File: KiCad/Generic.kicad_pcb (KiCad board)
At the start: 2 copper layers, 19 x 29 mm, 16 parts, among them J1 Connector, J2 USB-C, J3 VBUS, U1 ESP32-WROOM-32, U2 FT231XQ

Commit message: Improve fab diagram
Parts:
- moved Reg1 0.75 mm to (125.2, 107.5)
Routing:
- net GND: track 82.4 -> 85.7 mm
- net +3V3: track 74.9 -> 75.9 mm

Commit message: Slight tidy of tracks
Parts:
- J1: footprint RevK:Molex_MiniSPOX_H6RA -> RevK:Molex_MiniSPOX_H6RA_0.1
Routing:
- net O: track 18.4 -> 34.4 mm
- net EN: track 46.8 -> 32.0 mm
- net GND: track 85.7 -> 95.4 mm
- net Net-(U1-Pad13): track 3.91 -> 0.00 mm, vias 1 -> 0
- net +3V3: track 75.9 -> 74.6 mm
- net IO4: track 12.7 -> 13.4 mm
- net IO3: track 8.79 -> 9.42 mm
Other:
- board text added: "2021-05-11"
- board text added: "Link to DC"
- board text removed: "Link to 5V"

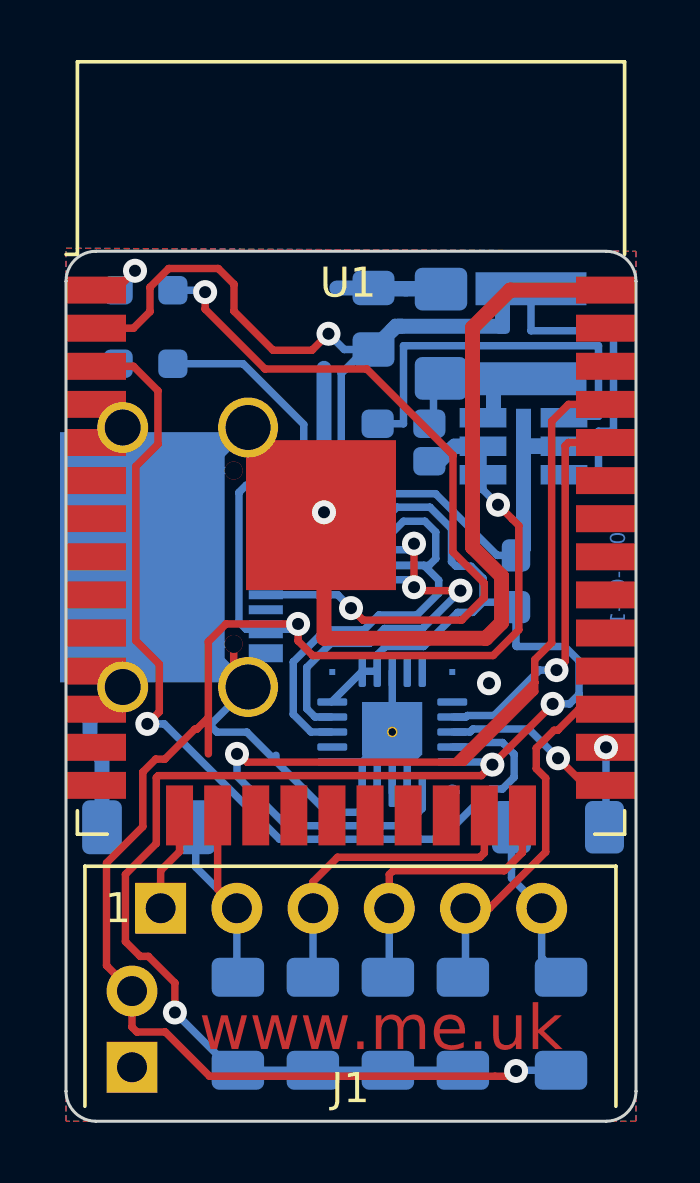
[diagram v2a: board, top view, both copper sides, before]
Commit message: Reworked for ULP pins and ADC pins
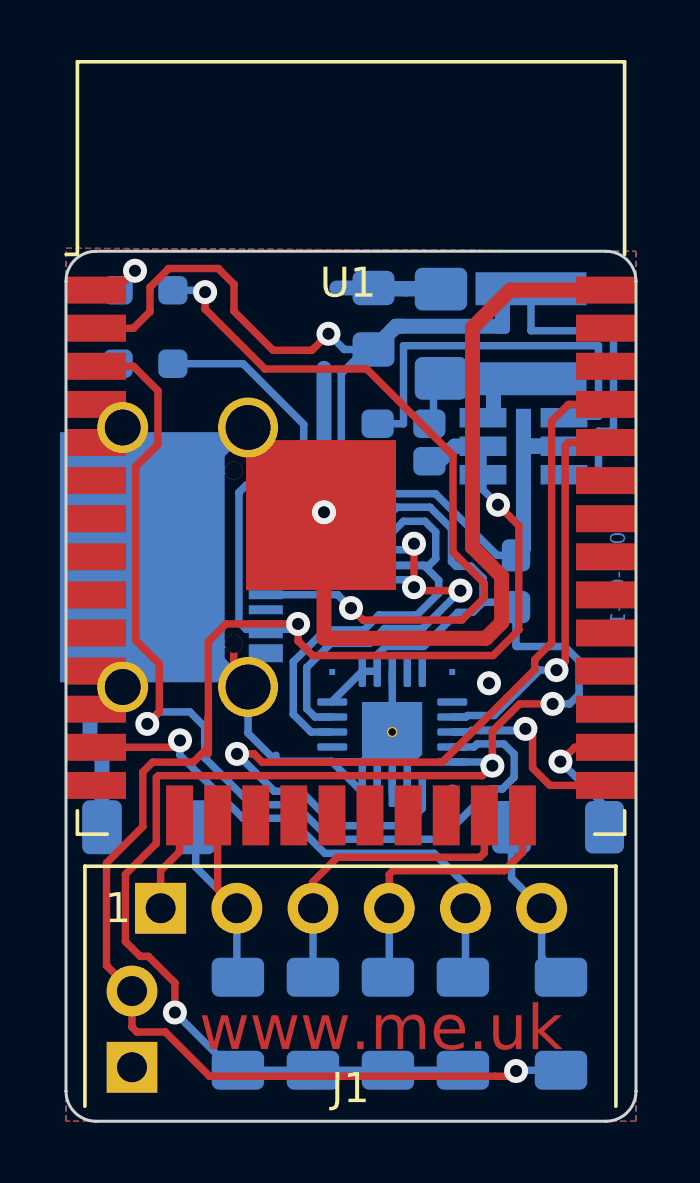
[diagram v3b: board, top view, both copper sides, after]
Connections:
- U1 pad 13: Net-(U1-Pad13) -> IO4
- U1 pad 27: IO4 -> Net-(U1-Pad27)
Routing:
- net IO4: track 13.4 -> 19.0 mm, vias 0 -> 1
- net O: track 34.4 -> 29.8 mm
- net GND: track 95.4 -> 92.9 mm
- net GPIO0: track 5.92 -> 8.30 mm
- net IO5: track 2.69 -> 4.51 mm
- net EN: track 32.0 -> 32.9 mm
- net +3V3: track 74.6 -> 75.3 mm
- net VBUS: track 57.8 -> 58.4 mm
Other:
- board text added: "14"
- board text removed: "16"

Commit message: Multi size pads with no solder past for user fit passives.
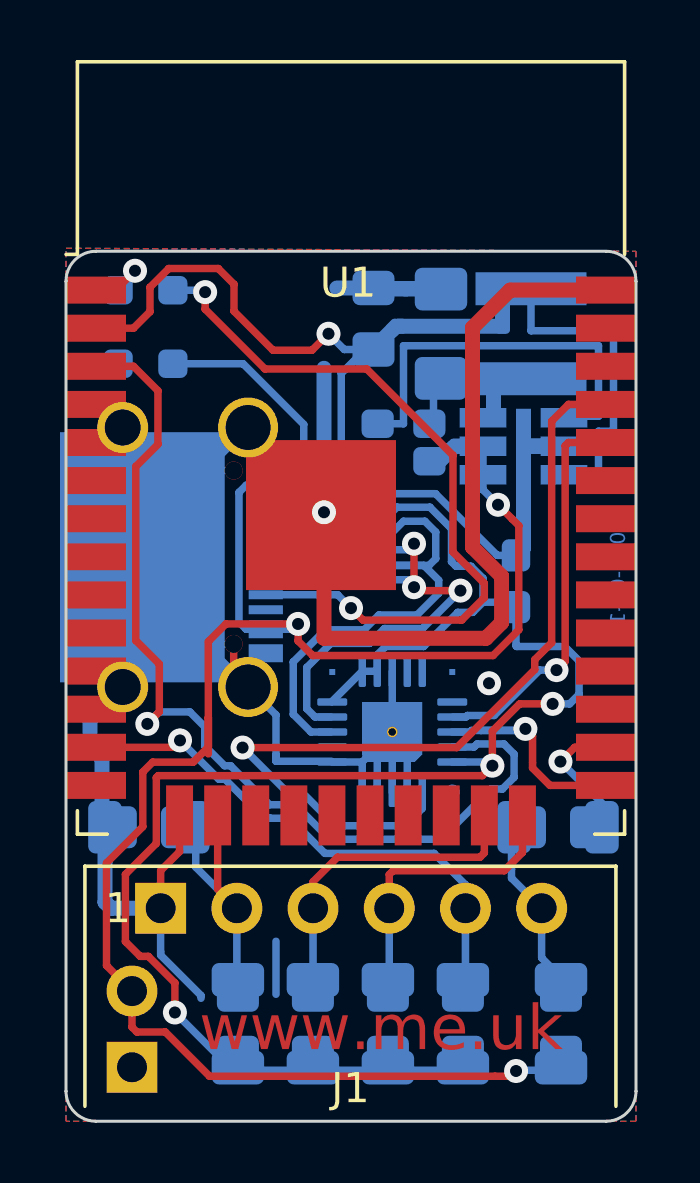
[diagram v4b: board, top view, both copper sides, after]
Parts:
- C1: footprint Capacitor_SMD:C_1206_3216Metric_Pad1.33x1.80mm_HandSolder -> RevK:Pad_1206_0805_NF
- R1, R2, R3, R4, R5, R6: footprint Resistor_SMD:R_1206_3216Metric_Pad1.30x1.75mm_HandSolder -> RevK:Pad_1206_0805_NF
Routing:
- net GND: track 92.9 -> 101.2 mm
- net O: track 29.8 -> 29.2 mm
